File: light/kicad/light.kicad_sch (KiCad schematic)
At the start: 74 parts, among them U1 FT4232H, U2 SN74AVC4T774RSVR, U3 SN74AVC4T774RSVR, U4 SN74AVC4T774RSVR, U5 SN74AVC4T774RSVR, U6 74AHC595

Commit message: kicad: added clocks, vregs, and other power routings
2025/09/01

1. Follow Demo board design and datasheet
        - Change L1, L2 to 600R/0.5A
2. 5V -> 3.3V LDO
	- Add U7, C23, C24
3. Getting power from host by 5.1k RD on CC.
	- Add R30 5.1k on CC1 of USB-C Receptacle
4. A method for being provider or receiver of 5V of Target device Provider path: 12k Rp for 5V@1.5A
	- Add SW1
	- Remove R5 on VCONN
	- Add R5 12k on SW
	- Change R4 to 5.1K."
5. Prioritizing Host 5V as default
	- Add D1, Q1, R31
6. Add power switch for 5V path output
	- Add U9, C31, C32
7. External Clock for FT4232
	- Add C27, C28, Y1
8. EC_VREF (3.3v) LDO
	- Add U8, C25, C26
9. Channel C and D don't have GPIO function.
	- "Move AP_UART_VREF_FORCE_3.3 to GPIO_L2 (but maybe we don't need it)"
10. LDO for SPI 3.3V and 1.8V
	- Add U11, C29, C30
11. Prevent activating SPI 3.3V and 1.8V at the same time.
	- Add U10(XOR), U12(AND), U13(AND)
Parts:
- added C23, C24: 10uF, Capacitor_SMD:C_0603_1608Metric, symbol Device:C
- added D1: D_Schottky, symbol Device:D_Schottky
- added Q1: PMOS, symbol Simulation_SPICE:PMOS
- added R30: 5.1k, symbol Device:R_US
- added R31: 2.2K, symbol Device:R_US
- added SW1: Slide Switch, Button_Switch_SMD:Nidec_Copal_CAS-120A, symbol Switch:SW_Nidec_CAS-120A1
- added U7: TLV75533PDBV, Package_TO_SOT_SMD:SOT-23-5, symbol Regulator_Linear:TLV75533PDBV
- L1, L2: value L_Ferrite -> 600R_0.5A
- R4: value 22k -> 5.1k
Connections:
- net 3.3V: now also C23.1, U7.5 (OUT)
- net CCD_VBUS: now also R5.2, Q1.1 (D); no longer R4.1, R5.1
- net GND: now also R4.2, C23.2, C24.2, R30.1, U7.2 (GND)
- net HOST_VBUS: now also D1.2 (A)
- net at DUT_CCD.A5 (CC): now also SW1.2 (B); no longer R5.2
- net at DUT_CCD.B5 (VCONN): no longer R4.2
- net Host_DM: now reaches U1.7 (DM)
- net Host_DM: now also HOST.A7 (D-), HOST.B7 (D-)
- net Host_DP: now reaches U1.8 (DP)
- net Host_DP: now also HOST.A6 (D+), HOST.B6 (D+)
- net at HOST.A5 (CC1): now also R30.2
- new net: Q1.2 (G), R31.1
- new net: C24.1, D1.1 (K), Q1.3 (S), R31.2, U7.1 (IN), U7.3 (EN)
- new net: R5.1, SW1.1 (C)
- new net: R4.1, SW1.3 (A)
- no-connect marks 15 -> 27
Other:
- note added: "Lilac: 3.3V Sunflower: 3.3V Marigold: 3.3V Iris: 3.3V Azalea: 3.3V Banshee: 3.3V ADL: 3.3V TGL: 3.3V Lotus: 3.3V Tulip: 3.3V"
- note added: "SW1: R5 = Providing power to target device R4 = Sinking power from target device (Default)"
- note added: "TODO: How to identify 1.8 or 3.3V system Lilac: 1.8V Marigold: 1.8V Azalea: 1.8V Lotus: 1.8V Tulip: 1.8V ADL: 3.3V Sunflower:3.3V Iris: 3.3V Banshee: 3.3V TGL: 3.3V"
- moved on the sheet: C22, LED_AP_UART, LED_AP_VREF, LED_EC_UART, LED_EC_VREF, LED_JTAG, LED_SPI, LED_SPI_VREF, R10, R11, R12, R13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

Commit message: kicad: Simplify Design and Correct Errors
2025/10/07

1. Add R33, R34, R35, R36 on USB+/- for banshee
2. Remove Q1, R31, D1
3. Add R29, Change U5 from 4 bit level shifter to OD buffer.
4. Remove netname AP_UART_VREF_FORCE_3.3 due to no need anymore.
5. Remove SW1, change R4 to 5.1K on CC and tie to GND, R32 to VCONN and tie to GND.
6. Change R27 to 1k from 100ohm
7. Remove U10(XOR), U12(AND), U13(AND)
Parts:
- removed C20, C21: 100nF, Capacitor_SMD:C_0603_1608Metric, symbol Device:C
- removed D1: D_Schottky, symbol Device:D_Schottky
- removed Q1: PMOS, symbol Simulation_SPICE:PMOS
- removed SW1: Slide Switch, Button_Switch_SMD:Nidec_Copal_CAS-120A, symbol Switch:SW_Nidec_CAS-120A1
- removed U5: SN74AVC4T774RSVR, RSV0016A, symbol SN74AVC4T774RSVR:SN74AVC4T774RSVR
- added C25, C26: 10uF, Capacitor_SMD:C_0603_1608Metric, symbol Device:C
- added C27, C28: 27pF, symbol Device:C
- added C29, C30: 1uF, Capacitor_SMD:C_0603_1608Metric, symbol Device:C
- added R32: 5.1k, symbol Device:R_US
- added R33, R34, R35, R36: 0, symbol Device:R_US
- added U11: TLV7103318DDSE, Package_SON:WSON-6_1.5x1.5mm_P0.5mm, symbol Regulator_Linear:TLV7113318DDSE
- added U14, U5: 74LVC1G07, symbol 74xGxx:74LVC1G07
- added U8: TLV75533PDBV, Package_TO_SOT_SMD:SOT-23-5, symbol Regulator_Linear:TLV75533PDBV
- added U9: 93LCxxBxxOT, Package_TO_SOT_SMD:SOT-23-6, symbol Memory_EEPROM:93LCxxBxxOT
- added Y1: 12MHz, symbol Device:Crystal
- JECDB: value 5034801000 -> JXT_FP241AH-010GAAM
- JPD: value 5034800600 -> ACES_50521-00641-P01
- JSPI: value 5034800600 -> HEFEN_AFC20-S06FIA-R0
- R27, R29: value 100 -> 1k
- R31: value 2.2K -> 2k
- R5: value 56k -> 10k
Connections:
- net 3.3V: now also R29.1, R5.1, U14.5 (VCC), U5.5 (VCC), U9.6 (VCC)
- net AP_SPI_VREF: now also C30.1, U11.5 (OUT2), U11.6 (OUT1)
- net CCD_VBUS: now also C25.1, U8.1 (IN), U8.3 (EN); no longer R5.2
- net EC_VREF: now also C26.1, U8.5 (OUT)
- net EECLK: now also U9.4 (CLK)
- net EECS: now also U9.5 (CS)
- net EEDATA: now also R31.1, U9.3 (DI)
- net FTDI_RX_AP_TX: now also U14.2; no longer R29.1
- net FTDI_RX_AP_TX_UNSHIFTED: now also R29.2, U14.4
- net FTDI_RX_EC_TX: now also R36.1
- net FTDI_TX_AP_RX_UNSHIFTED: now also U5.2
- net FTDI_TX_EC_RX: now also R35.1
- net GND: now also C25.2, C26.2, C27.1, C28.2, C29.2, C30.2, R32.2, U11.4 (GND), U14.3 (GND), U5.3 (GND), U8.2 (GND), U9.2 (GND)
- net HOST_VBUS: now also C24.1, U7.1 (IN), U7.3 (EN), C29.1, U11.2 (VIN)
- net Host_DM: now also R33.1; no longer HOST.A7 (D-), HOST.B7 (D-)
- net Host_DP: now also R34.1; no longer HOST.A6 (D+), HOST.B6 (D+)
- net LED_JTAG: now also U6.15 (QA)
- net LED_SPI: now also U6.2 (QC)
- net at R28.2: now also U5.4
- net at DUT_CCD.A5 (CC): now also R4.1
- net at DUT_CCD.B5 (VCONN): now also R32.1
- net at U1.2 (OSCI): now also C28.1, Y1.2
- net at U1.3 (OSCO): now also C27.2, Y1.1
- net AP_UART_VREF_FORCE_3.3: no longer names the net of U1.55 (DDBUS4)
- new net: R31.2, R5.2, U9.1 (DO)
- new net Host_DM_CONN: HOST.A7 (D-), HOST.B7 (D-), R33.2, R35.2
- new net Host_DP_CONN: HOST.A6 (D+), HOST.B6 (D+), R34.2, R36.2
- new net SPI_VREF_FORCE_1.8_OUT: U11.3 (EN2)
- new net SPI_VREF_FORCE_3.3_OUT: U11.1 (EN1)
- no-connect marks 27 -> 42
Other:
- note added: "TODO: Lilac: 1.8V Marigold: 1.8V Azalea: 1.8V Lotus: 1.8V Tulip: 1.8V ADL: 3.3V Sunflower:3.3V Iris: 3.3V Banshee: 3.3V TGL: 3.3V"
- note removed: "SW1: R5 = Providing power to target device R4 = Sinking power from target device (Default)"
- note removed: "TODO: How to identify 1.8 or 3.3V system Lilac: 1.8V Marigold: 1.8V Azalea: 1.8V Lotus: 1.8V Tulip: 1.8V ADL: 3.3V Sunflower:3.3V Iris: 3.3V Banshee: 3.3V TGL: 3.3V"
- note removed: "TODO: implement"
- moved on the sheet: C1, C10, C11, C12, C13, C14, C15, C16, C17, C18, C19, C2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

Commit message: kicad: Add MUX for JTAG/SWD, Fix SPI netname error
2025/10/13

1. Remove R15, LED_AP_VREF and "AP_UART_VREF" net name
2. Adding Test points(TP2~TP18) to replace NC pins of U1 and U6
3. Adding footprint of parts
4. Correct Netname errors.
	SPI_VREF_FORCE_3.3_OUT -> SPI_VREF_FORCE_3.3
	SPI_VREF_FORCE_1.8_OUT -> SPI_VREF_FORCE_1.8
	SPI_OE_N -> FTDI_SPI_OE_N
5. DNC R35, R36
6. Add R15, R37, for isolating Banshee path and normal path
7. Add U10, C20, Netname "JTAG_SWD_SEL", Remove R22, R23, R24.
8. Change netname AP_UART_VREF to JTAG_SWD_SEL for LED indicator
9. Chnage JPD, JSPI PN to MOLEX_5051100692, JECDB to MOLEX_5051101097, which are similar to what Compal used.
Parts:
- removed LED_AP_VREF: WHITE, symbol Device:LED
- removed NT3: NetTie_2, symbol Device:NetTie_2
- removed R23, R24: 0, symbol Device:R_US
- added C20: 0.1uF, Capacitor_SMD:C_0603_1608Metric, symbol Device:C
- added LED_PD: WHITE, symbol Device:LED
- added R37: 0, symbol Device:R_US
- added TP10, TP11, TP12, TP13, TP14, TP15, TP16, TP17, TP18, TP2, TP3, TP4, TP5, TP6, TP7, TP8, TP9: TestPoint, symbol Connector:TestPoint
- added U10: TMUX1574RSV, Package_DFN_QFN:UQFN-16_1.8x2.6mm_P0.4mm, symbol Analog_Switch:TMUX1574RSV
- DUT_CCD: footprint (none) -> USB4155
- HOST: footprint (none) -> USB4080
- JECDB: value JXT_FP241AH-010GAAM -> MOLEX_5051101097; footprint CON_5034801000_MOL -> (none)
- JPD: value ACES_50521-00641-P01 -> MOLEX_5051100692; footprint 503480-0600_MOL -> 5051100692
- JSPI: value HEFEN_AFC20-S06FIA-R0 -> MOLEX_5051100692; footprint 503480-0600_MOL -> 5051100692
- R35, R36: now not fitted
- U6: value 74AHC595 -> SN74AHC595QWBQBRQ1; footprint (none) -> SN74AHC595QWBQBRQ1
- U9: value 93LCxxBxxOT -> 93LC56BT-I/OT
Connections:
- net AP_UART_VREF is gone; now on net JTAG_SWD_SEL: R15.2
- net SPI_OE_N is gone; now on net FTDI_SPI_OE_N: U1.34 (BDBUS7)
- net SPI_VREF_FORCE_1.8_OUT is gone; now on net SPI_VREF_FORCE_1.8: U11.3 (EN2)
- net SPI_VREF_FORCE_3.3_OUT is gone; now on net SPI_VREF_FORCE_3.3: U11.1 (EN1)
- net 3.3V: now also C20.1, U10.14 (VDD)
- net EC_JTAG_TCK: now also U10.16 (S1A)
- net EC_JTAG_TDO: now also U10.9 (S3A)
- net EC_JTAG_TMS: now also U10.12 (S4A); no longer R22.1
- net FTDI_RX_EC_TX: now also R37.2; no longer DUT_CCD.B8 (SBU2), R36.1
- net FTDI_TX_EC_RX: now also R22.2; no longer DUT_CCD.A8 (SBU1), R35.1
- net GND: now also C20.2, LED_PD.1 (K), U10.13 (~{EN}), U10.6 (GND)
- net JTAG_TCK: now also U10.2 (D1)
- net JTAG_TDI: now also U10.5 (D2); no longer R20.2
- net JTAG_TDO: now also U10.7 (D3); no longer R21.2
- net JTAG_TMS: now also U10.10 (D4); no longer R22.2
- net PD_SWCLK: now also U10.1 (S1B)
- net at U6.1 (QB): now also TP16.1
- net at U6.3 (QD): now also TP17.1
- net at U6.9 (QH'): now also TP18.1
- net at R15.1: now also LED_PD.2 (A)
- net JTAG_SWD_SEL: now reaches U1.22 (ADBUS5)
- net JTAG_SWD_SEL: now also U10.15 (SEL)
- net at U1.23 (ADBUS6): now also TP2.1
- net at U1.24 (ADBUS7): now also TP3.1
- net at U1.33 (BDBUS6): now also TP4.1
- net at U1.36 (~{SUSPEND}): now also TP15.1
- net at U1.41 (CDBUS3): now also TP5.1
- net at U1.44 (CDBUS5): now also TP6.1
- net at U1.45 (CDBUS6): now also TP7.1
- net at U1.46 (CDBUS7): now also TP8.1
- net at U1.53 (DDBUS2): now also TP9.1
- net at U1.54 (DDBUS3): now also TP10.1
- net at U1.55 (DDBUS4): now also TP11.1
- net at U1.57 (DDBUS5): now also TP12.1
- net at U1.58 (DDBUS6): now also TP13.1
- net at U1.59 (DDBUS7): now also TP14.1
- new net: R20.2, U10.4 (S2B)
- new net: R21.2, U10.8 (S3B)
- new net FTDI_RX_EC_TX_CONN: DUT_CCD.B8 (SBU2), R36.1, R37.1
- new net FTDI_TX_EC_RX_CONN: DUT_CCD.A8 (SBU1), R22.1, R35.1
- no-connect marks 42 -> 26
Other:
- note added: "If connect to Banshee: DNP R22 & R37"
- note added: "If connect to Banshee: DNP R33 & R34 Populate R35 & R36"
- note added: "JTAG_SWD_SEL L: EC_JTAG H: PD_SWD"
- note added: "TODO: Dogwood: 1.8V Lilac: 1.8V Marigold: 1.8V Azalea: 1.8V Lotus: 1.8V Tulip: 1.8V ADL: 3.3V Sunflower:3.3V Iris: 3.3V Banshee: 3.3V TGL: 3.3V"
- note removed: "TODO: Check if any of these EC_JTAG are supposed to be bidir."
- note removed: "TODO: Lilac: 1.8V Marigold: 1.8V Azalea: 1.8V Lotus: 1.8V Tulip: 1.8V ADL: 3.3V Sunflower:3.3V Iris: 3.3V Banshee: 3.3V TGL: 3.3V"
- moved on the sheet: C1, C10, C11, C12, C13, C2, C22, C27, C28, C3, C4, C5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

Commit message: kicad: Remove JTAG MUX and add Cortex20-10 adaptor
2025/10/15

1. Remove U10, C20, Netname "JTAG_SWD_SEL"
2. Roll back design of SWDIO/JTAG(adding back R20, R21, TP1, R15, R22, R23)
3. Add JDB10 and JDB20
4.  Change JSPI and JPD to HRS_FH19C-6S-0.5SH
5. Change JECDB to Cvilux_CF35102D0RE-NH
6. Add TP19, TP20, TP21, TP22, TP23 on Unused pin of JTAG
7. Remove JTAG_SWD LED
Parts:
- removed C20: 0.1uF, Capacitor_SMD:C_0603_1608Metric, symbol Device:C
- removed LED_PD: WHITE, symbol Device:LED
- removed U10: TMUX1574RSV, Package_DFN_QFN:UQFN-16_1.8x2.6mm_P0.4mm, symbol Analog_Switch:TMUX1574RSV
- added JDB10: Conn_ARM_JTAG_SWD_10, symbol Connector:Conn_ARM_JTAG_SWD_10
- added JDB20: Conn_ARM_JTAG_SWD_20, symbol Connector:Conn_ARM_JTAG_SWD_20
- added NT3: NetTie_2, symbol Device:NetTie_2
- added R23, R24: 0, symbol Device:R_US
- added TP1, TP19, TP20, TP21, TP22, TP23: TestPoint, symbol Connector:TestPoint
- JECDB: value MOLEX_5051101097 -> Cvilux_CF35102D0RE-NH
- JPD, JSPI: value MOLEX_5051100692 -> HRS_FH19C-6S-0.5SH; footprint 5051100692 -> (none)
- R15: value 330 -> 0
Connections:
- net EC_JTAG_TCK: now also NT3.1, R23.1
- net EC_JTAG_TDO: now also R24.1
- net EC_JTAG_TMS: now also R15.1
- net GND: now also JDB10.3 (GND), JDB10.5 (GND), JDB10.9 (GNDDetect), JDB20.10 (GND), JDB20.12 (GND), JDB20.14 (GND), JDB20.16 (GND), JDB20.18 (GND), JDB20.20 (GND), JDB20.4 (GND), JDB20.6 (GND), JDB20.8 (GND)
- net JTAG_TCK: now also R23.2
- net JTAG_TDI: now also R20.2
- net JTAG_TDO: now also R21.2, R24.2
- net JTAG_TMS: now also R15.2
- net PD_SWCLK: now also NT3.2
- net JTAG_SWD_SEL: no longer names the net of U1.22 (ADBUS5)
- net JTAG_SWD_SEL: now also TP1.1; no longer R15.2
- new net: JDB20.3 (~{TRST}), TP23.1
- new net: JDB20.19 (DBGACK/NC), TP20.1
- new net: JDB20.17 (DBGRQ/NC), TP21.1
- new net: JDB20.11 (RTCK), TP22.1
- new net: JDB20.2 (VCC/NC), TP19.1
- new net: JDB10.1 (VTref), JDB20.1 (VTREF)
- new net: JDB10.6 (SWO/TDO), JDB20.13 (TDO/SWO)
- new net: JDB10.10 (~{RESET}), JDB20.15 (~{SRST})
- new net: JDB10.8 (NC/TDI), JDB20.5 (TDI)
- new net: JDB10.2 (SWDIO/TMS), JDB20.7 (TMS/SWDIO)
- new net: JDB10.4 (SWCLK/TCK), JDB20.9 (TCK/SWCLK)
- no-connect marks 26 -> 24
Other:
- note removed: "JTAG_SWD_SEL L: EC_JTAG H: PD_SWD"

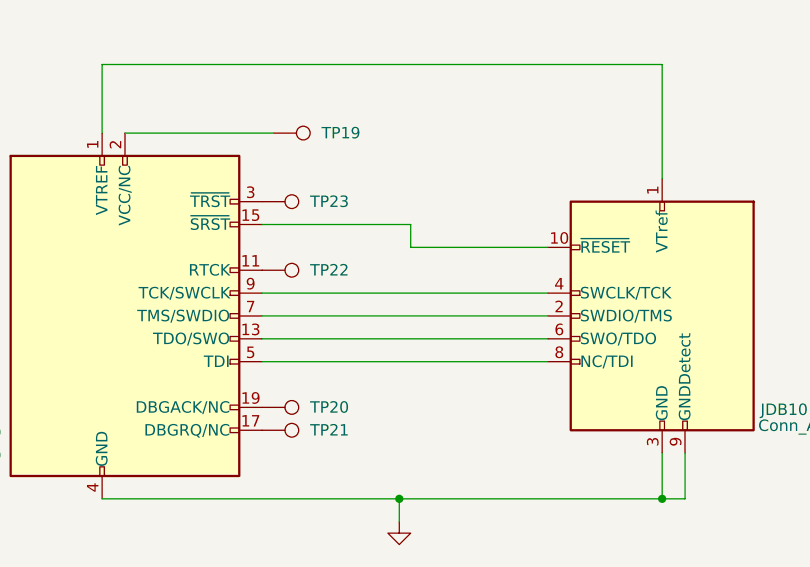
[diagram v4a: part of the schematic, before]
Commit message: kicad: Adding JTAG Connections
10/16

1. Add JTAG Connection between JDB10 and JDB20
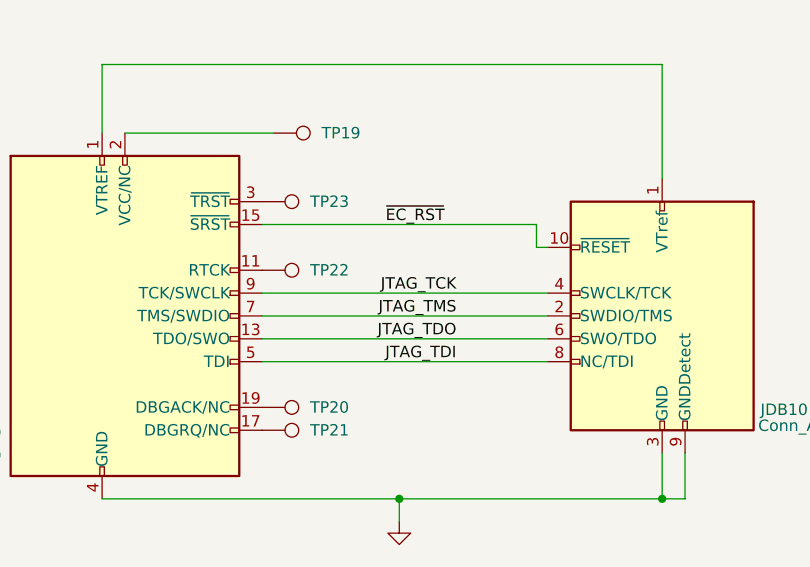
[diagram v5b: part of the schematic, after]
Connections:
- net JTAG_TCK: now also JDB10.4 (SWCLK/TCK), JDB20.9 (TCK/SWCLK)
- net JTAG_TDI: now also JDB10.8 (NC/TDI), JDB20.5 (TDI)
- net JTAG_TDO: now also JDB10.6 (SWO/TDO), JDB20.13 (TDO/SWO)
- net JTAG_TMS: now also JDB10.2 (SWDIO/TMS), JDB20.7 (TMS/SWDIO)
- net ~{EC_RST}: now also JDB10.10 (~{RESET}), JDB20.15 (~{SRST})
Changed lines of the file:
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@@
 	(wire
 		(pts
-			(xy 237.49 245.11) (xy 252.73 245.11)
+			(xy 251.46 245.11) (xy 252.73 245.11)
 		)
 		(stroke
@@
 	(wire
 		(pts
-			(xy 220.98 242.57) (xy 237.49 242.57)
+			(xy 220.98 242.57) (xy 251.46 242.57)
 		)
 		(stroke
@@
 	(wire
 		(pts
-			(xy 237.49 242.57) (xy 237.49 245.11)
+			(xy 251.46 242.57) (xy 251.46 245.11)
 		)
 		(stroke
@@
 		)
 	)
+	(label "~{EC_RST}"
+		(at 234.696 242.57 0)
+		(effects
+			(font
+				(size 1.27 1.27)
+			)
+			(justify left bottom)
+		)
+	)
 	(label "AP_SPI_CLK"
 		(at 375.92 69.85 0)
@@
 		)
 	)
+	(label "JTAG_TDI"
+		(at 242.57 257.81 180)
+		(effects
+			(font
+				(size 1.27 1.27)
+			)
+			(justify right bottom)
+		)
+	)
 	(label "FTDI_RTS"
 		(at 171.45 128.27 0)
@@
 		)
 	)
+	(label "JTAG_TMS"
+		(at 242.57 252.73 180)
+		(effects
+			(font
+				(size 1.27 1.27)
+			)
+			(justify right bottom)
+		)
+	)
 	(label "Host_DM"
 		(at 99.06 102.87 0)
@@
 		)
 	)
+	(label "JTAG_TCK"
+		(at 242.57 250.19 180)
+		(effects
+			(font
+				(size 1.27 1.27)
+			)
+			(justify right bottom)
+		)
+	)
 	(label "FTDI_TX_AP_RX"
 		(at 308.61 184.15 180)
@@
 		)
 	)
+	(label "JTAG_TDO"
+		(at 242.57 255.27 180)
+		(effects
+			(font
+				(size 1.27 1.27)
+			)
+			(justify right bottom)
+		)
+	)
